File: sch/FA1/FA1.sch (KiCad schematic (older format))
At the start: 5 parts, among them J1 240V mains, J2 Cellular Antenna, J3 DMX Out, U1 FP1 sub-assembly, U2 PS-05-5

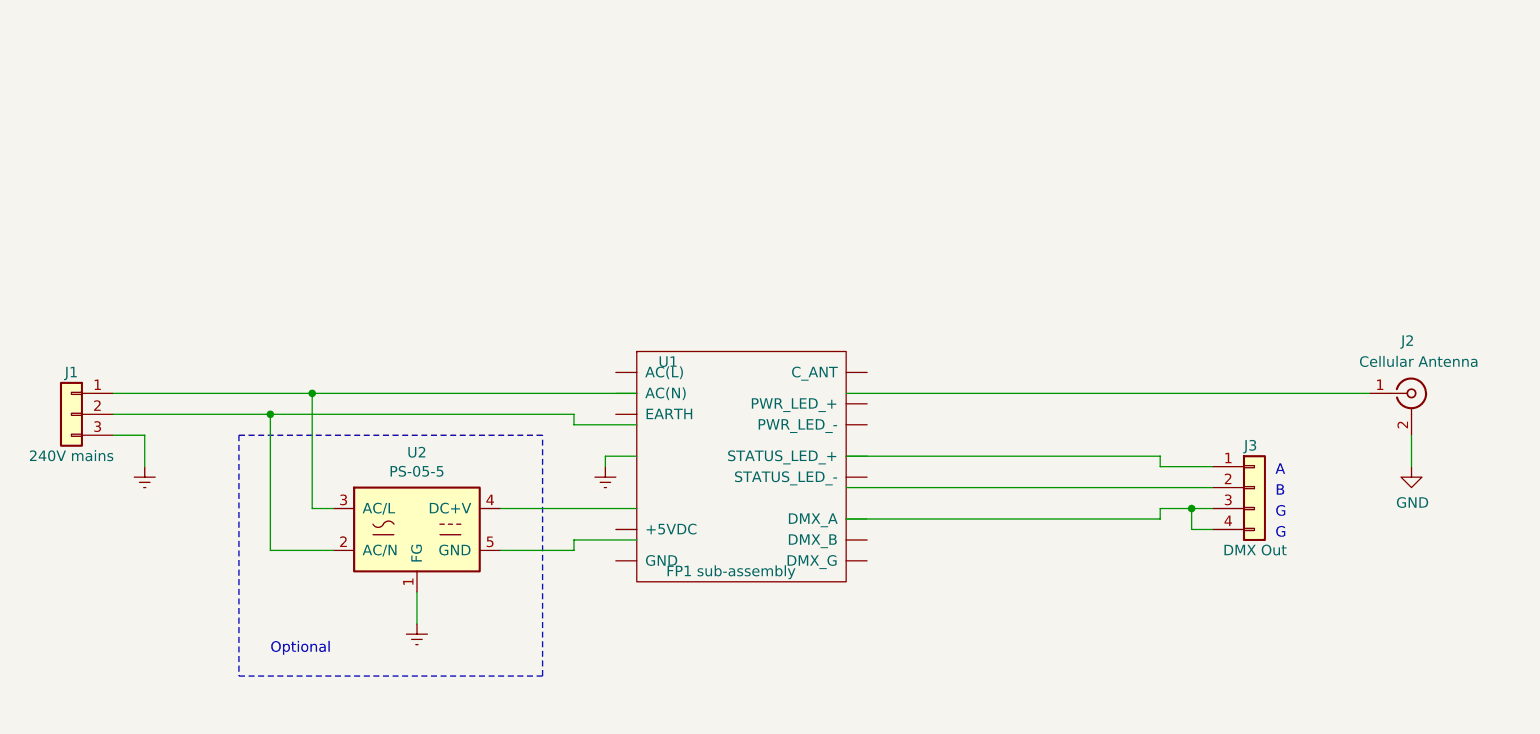
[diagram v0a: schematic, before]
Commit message: Completed BOMs and changed module connector name to 'Faraday_module'
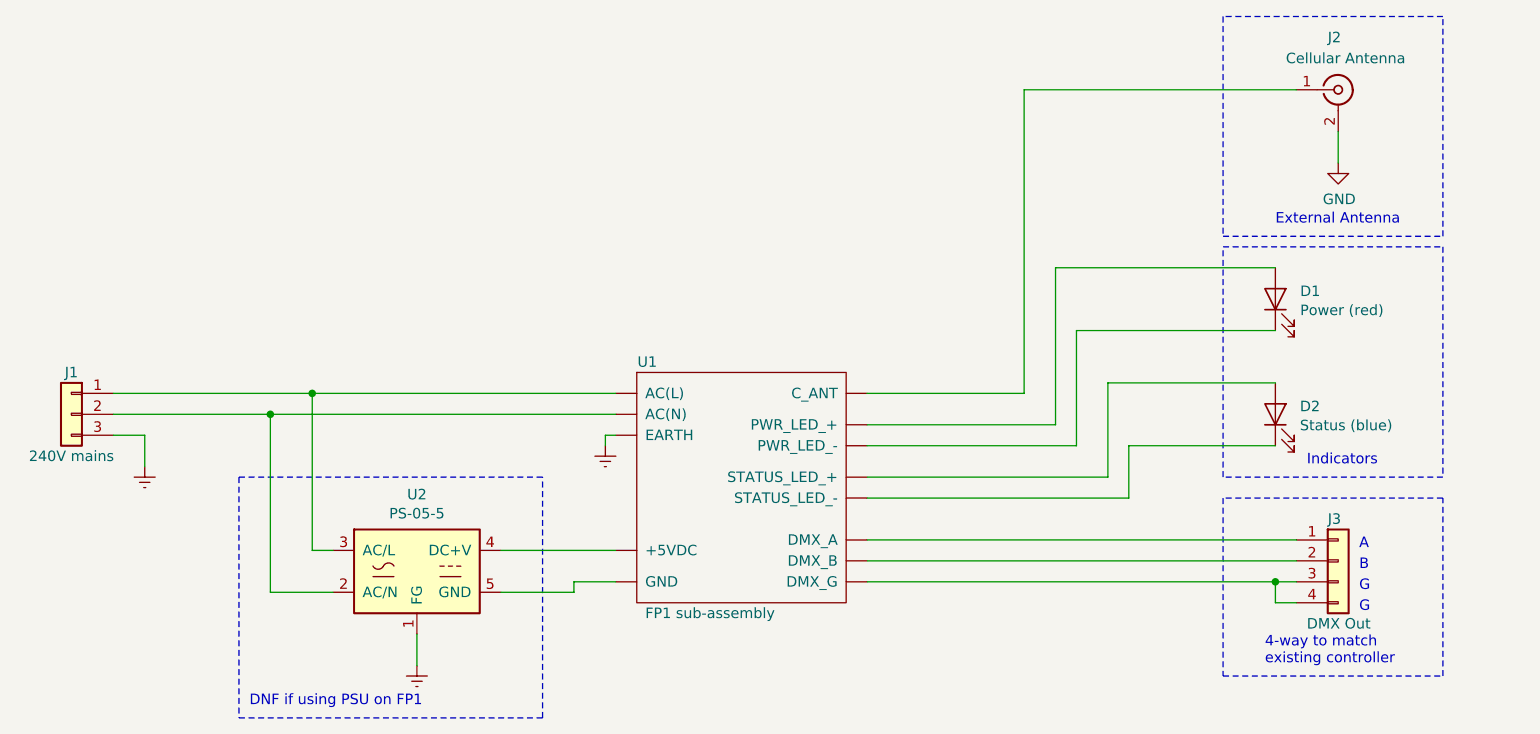
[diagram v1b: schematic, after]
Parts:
- added D1: Power (red), symbol Device:LED
- added D2: Status (blue), symbol Device:LED
- U1: Manufacturer (none) -> NewieVentures; Order Number (none) -> FP1; Part Number (none) -> FP1; Supplier (none) -> NewieVentures
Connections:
- wire segments 31 -> 39
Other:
- note added: "4-way to match\nexisting controller"
- note added: "DNF if using PSU on FP1"
- note added: "External Antenna"
- note added: "Indicators"
- note removed: "Optional"
- moved on the sheet: J2, J3, U1, U2
